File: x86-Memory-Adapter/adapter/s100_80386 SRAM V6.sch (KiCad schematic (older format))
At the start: 71 parts, among them P1 CONN_1, P10 CPLD SPARE, P2 CONN_1, P20 S100_MALE, P3 CONN_1, P34 CONN_1, P35 CONN_1, P4 CONN_1, P5 CONN_20X2, P6 CONN_25X2, P7 XILINX CABLE2, P8 CONN_20X2, P9 CONN_20X2, U1 LDO_REG_7805, U10 74LVX3245, U11 74LVX3245, U12 74LVX3245, U13 74LVX3245, U14 XC9572XL-VQ44, U17 74F04, U2 74LVC573, U3 74LVC573, U4 74LVC573, U5 74LVC573, U6 74LVC573, U7 LM1086CS_TO252_DPAK, U8 74F14, U9 74LVX3245

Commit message: x86-Memory-Adapter: adapter JTAG chain jumper, mezzanine JTAG, CPLD spare header
Source: S100 4GB DRAM BOARD/S100 80386 SRAM DB Version 1/backups/24-04-2015 1921
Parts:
- removed P10: CPLD SPARE, symbol CONN_4
- added P10: CPLD Spare, ~, symbol CONN_2
- added P11: CONN_2X2, symbol CONN_2X2
- added P12: JTAG CHAIN, symbol CONN_2X2
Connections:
- net labels added: FPGA_TDI, FPGA_TDO, TDO_1
- wire segments 713 -> 718
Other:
- note added: "Bridge 2-4 if only CPLD in chain\nBridge 1-2 & 3-4 if FPGA board in chain"
- moved on the sheet: R8, R9
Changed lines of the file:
@@
 Sheet 1 1
 Title "noname.sch"
-Date "23 apr 2015"
+Date "24 apr 2015"
 Rev ""
 Comp ""
@@
 GND
 Text Label 10800 19500 0    60   ~ 0
-CPLD1_TDO
+TDO_1
 Text Label 10800 19600 0    60   ~ 0
 CPLD1_TDI
@@
 	18000 16600 18350 16600
 Wire Wire Line
-	21800 17200 22350 17200
-Wire Wire Line
 	9750 19600 9000 19600
 Wire Wire Line
@@
 Wire Wire Line
 	13250 4450 13100 4450
-Text Label 23050 17200 0    60   ~ 0
+Text Label 22750 18400 0    60   ~ 0
 V3.3
 Text Label 21950 15150 0    60   ~ 0
@@
 V3.3
 Wire Wire Line
-	19800 18150 19800 19350
-Wire Wire Line
 	19500 18150 19500 18450
 Wire Wire Line
@@
 Text Label 17750 14550 2    60   ~ 0
 CPLD_P34
-Text Label 15950 9550 2    60   ~ 0
+Text Label 16650 9550 2    60   ~ 0
 CPLD_P44
 Text Label 14250 13350 0    60   ~ 0
@@
 Text Label 17750 17200 2    60   ~ 0
 CPLD_P8
-Text Label 15950 9250 2    60   ~ 0
-CPLD_P7
 Text Label 11700 5150 2    60   ~ 0
-CPLD_P6
+CPLD_P7
 Text Label 11700 5050 2    60   ~ 0
-CPLD_P5
+CPLD_P6
 Text Label 11700 4950 2    60   ~ 0
-CPLD_P3
+CPLD_P5
 Text Label 11700 4850 2    60   ~ 0
+CPLD_P3
+Text Label 11700 4750 2    60   ~ 0
 CPLD_P2
 Text Label 14250 11050 0    60   ~ 0
 CPLD_P1
-Text Label 15950 9350 2    60   ~ 0
+Text Label 13800 5150 0    60   ~ 0
 CPLD_P8
 Text Label 17750 19150 2    60   ~ 0
@@
 Text Label 22750 16150 0    60   ~ 0
 CPLD_P33
-Text Label 15950 9450 2    60   ~ 0
+Text Label 16650 9350 2    60   ~ 0
 CPLD_P23
 Text Label 20650 12050 2    60   ~ 0
@@
 	13850 13350 14250 13350
 Wire Wire Line
-	11700 4850 12300 4850
+	11700 4750 12300 4750
 Wire Wire Line
-	12300 4950 11700 4950
+	12300 4850 11700 4850
 Wire Wire Line
-	11700 5050 12300 5050
+	11700 4950 12300 4950
 Wire Wire Line
-	12300 5150 11700 5150
-$Comp
-L CONN_4 P10
-U 1 1 5539C2C9
-P 16550 9400
-F 0 "P10" V 16500 9400 50  0000 C CNN
-F 1 "CPLD SPARE" V 16600 9400 50  0000 C CNN
-F 2 "" H 16550 9400 60  0000 C CNN
-F 3 "" H 16550 9400 60  0000 C CNN
-	1    16550 9400
-	1    0    0    -1
-$EndComp
+	12300 5050 11700 5050
 Wire Wire Line
-	16200 9250 15950 9250
+	11700 5150 12300 5150
 Wire Wire Line
-	15950 9350 16200 9350
+	13100 5150 13800 5150
 Wire Wire Line
-	16200 9450 15950 9450
+	16900 9350 16650 9350
 Wire Wire Line
-	15950 9550 16200 9550
+	16650 9550 16900 9550
 $Comp
 L CP C33
@@
 L R R8
 U 1 1 553A0DDD
-P 21550 15150
-F 0 "R8" V 21630 15150 50  0000 C CNN
-F 1 "3v" V 21550 15150 50  0000 C CNN
-F 2 "" H 21550 15150 60  0001 C CNN
-F 3 "" H 21550 15150 60  0001 C CNN
-	1    21550 15150
+P 21500 14950
+F 0 "R8" V 21580 14950 50  0000 C CNN
+F 1 "3v" V 21500 14950 50  0000 C CNN
+F 2 "" H 21500 14950 60  0001 C CNN
+F 3 "" H 21500 14950 60  0001 C CNN
+	1    21500 14950
 	0    1    1    0
 $EndComp
-Wire Wire Line
-	21300 15150 20700 15150
-Wire Wire Line
-	21950 15150 21800 15150
 $Comp
 L R R9
 U 1 1 553A1441
-P 22600 17200
-F 0 "R9" V 22680 17200 50  0000 C CNN
-F 1 "3v" V 22600 17200 50  0000 C CNN
-F 2 "" H 22600 17200 60  0001 C CNN
-F 3 "" H 22600 17200 60  0001 C CNN
-	1    22600 17200
+P 22250 18750
+F 0 "R9" V 22330 18750 50  0000 C CNN
+F 1 "3v" V 22250 18750 50  0000 C CNN
+F 2 "" H 22250 18750 60  0001 C CNN
+F 3 "" H 22250 18750 60  0001 C CNN
+	1    22250 18750
 	0    1    1    0
 $EndComp
 Wire Wire Line
-	23050 17200 22850 17200
-Wire Wire Line
-	19800 19850 19800 20000
-Wire Wire Line
 	9500 20550 9500 20500
 Connection ~ 9500 20500
@@
 Text Label 11850 21000 0    60   ~ 0
 GND
+Text Label 21750 21050 2    60   ~ 0
+CPLD1_TCK
+Text Label 21750 20900 2    60   ~ 0
+CPLD1_TMS
+Text Label 21550 20500 2    60   ~ 0
+FPGA_TDI
+Text Label 22700 20500 0    60   ~ 0
+CPLD1_TDO
+Text Label 22700 20400 0    60   ~ 0
+TDO_1
+$Comp
+L CONN_2X2 P12
+U 1 1 553A766D
+P 22100 20450
+F 0 "P12" H 22100 20600 50  0000 C CNN
+F 1 "JTAG CHAIN" H 22110 20320 40  0000 C CNN
+F 2 "" H 22100 20450 60  0000 C CNN
+F 3 "" H 22100 20450 60  0000 C CNN
+	1    22100 20450
+	1    0    0    -1
+$EndComp
+Text Label 21550 20400 2    60   ~ 0
+FPGA_TDO
+Wire Wire Line
+	22700 20400 22500 20400
+Wire Wire Line
+	22700 20500 22500 20500
+Wire Wire Line
+	21700 20400 21550 20400
+Wire Wire Line
+	21550 20500 21700 20500
+Text Notes 21500 20050 0    60   ~ 0
+Bridge 2-4 if only CPLD in chain\nBridge  1-2 & 3-4 if FPGA board in chain
+Text Label 13100 5700 0    60   ~ 0
+CPLD1_TCK
+Text Label 13100 5600 0    60   ~ 0
+CPLD1_TMS
+Text Label 12150 5700 2    60   ~ 0
+FPGA_TDI
+Text Label 12150 5600 2    60   ~ 0
+FPGA_TDO
+Wire Wire Line
+	12300 5600 12150 5600
+Wire Wire Line
+	12150 5700 12300 5700
+$Comp
+L CONN_2X2 P11
+U 1 1 553A8739
+P 12700 5650
+F 0 "P11" H 12700 5800 50  0000 C CNN
+F 1 "CONN_2X2" H 12710 5520 40  0000 C CNN
+F 2 "" H 12700 5650 60  0000 C CNN
+F 3 "" H 12700 5650 60  0000 C CNN
+	1    12700 5650
+	1    0    0    -1
+$EndComp
+Wire Wire Line
+	21800 17200 21900 17200
+Wire Wire Line
+	21900 17200 21900 18400
+Wire Wire Line
+	19800 18400 22750 18400
+Wire Wire Line
+	19800 18400 19800 18150
+Connection ~ 21900 18400
+Wire Wire Line
+	20700 15150 21950 15150
+$Comp
+L CONN_2 P10
+U 1 1 553AB388
+P 17250 9450
+F 0 "P10" V 17200 9450 40  0000 C CNN
+F 1 "CPLD Spare" V 17300 9450 40  0000 C CNN
+F 2 "~" H 17250 9450 60  0000 C CNN
+F 3 "~" H 17250 9450 60  0000 C CNN
+	1    17250 9450
+	1    0    0    -1
+$EndComp
 $EndSCHEMATC

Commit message: x86-Memory-Adapter: adapter LT3081 adjustable rail and 3.3V/5V source jumpers; first routing
Source: S100 4GB DRAM BOARD/S100 80386 SRAM DB Version 1/backups/25-04-2015 1211
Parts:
- added C12, C16, C2, C20, C23, C25, C5: 10 uF, symbol CP
- added K1: 3.3V, ~, symbol CONN_3
- added K2: 5V, ~, symbol CONN_3
- added P13: LT Output select, symbol CONN_6X2
- added R10: 500, symbol R
- added R11: 24.3K, symbol R
- added R12: 36.5K, symbol R
- added R13: 66.5K, symbol R
- added R14: 100, symbol R
- added R15: 30.1K, symbol R
- added R16: 49.9K, symbol R
- added R17: 100K, symbol R
- added R7: 4.53k, symbol R
- added U15: LDO_REG_7805, ~, symbol LDO_REG_7805
- added U16: LM1086CS, symbol LM1086CS
- added U18, U19: POWER_SELECT, symbol POWER_SELECT
- added U20: LT3081-TSSOP16, symbol LT3081-TSSOP16
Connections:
- net labels added: LM1086 out, LM7805 out, LTout
- wire segments 718 -> 825
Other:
- note added: "+3.3V from Power supply on Rail"
- note added: "+5V from Power supply on Rail"
- note added: "Optional"

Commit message: x86-Memory-Adapter: adapter power section simplified; routed board and gerbers
Source: S100 4GB DRAM BOARD/S100 80386 SRAM DB Version 1/backups/20-06-2015 1159 - need to move CPLD
The folder was made on 20-06-2015 but its files were last saved on 25-04-2015 (gerbers 14:47), so the commit carries the April date.
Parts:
- removed C2, C5: 10 uF, symbol CP
- removed R8, R9: 3v, symbol R
- removed U15: LDO_REG_7805, ~, symbol LDO_REG_7805
- removed U16: LM1086CS, symbol LM1086CS
- removed U18, U19: POWER_SELECT, symbol POWER_SELECT
- added R18: 300, symbol R
- R14: value 100 -> 1K
- U20: value LT3081-TSSOP16 -> LT3081
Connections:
- wire segments 825 -> 802
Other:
- note added: "TSSOP16"
- note removed: "+3.3V from Power supply on Rail"
- note removed: "+5V from Power supply on Rail"

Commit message: x86-Memory-Adapter: adapter CPLD moved to bottom; add general I/O, 23LC1024, select LED
Source: S100 4GB DRAM BOARD/S100 80386 SRAM DB Version 1/backups/21-06-2015 1724
Board partly re-routed after the move. The April gerbers are kept.
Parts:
- added C2: 0.1 uF, symbol C
- added D2: LED, LEDV, symbol LED
- added P14: GenIO_1, symbol CONN_6X2
- added P15: GenIO_2, symbol CONN_6X2
- added R19: 10k, symbol R
- added R20: 1K, symbol R
- added R21, R22, R23, R9: 10K, symbol R
- added R8: 330, symbol R
- added U15: ZZZZ1, symbol ZZZZ1
- added U16: ^^74LV244, ~, symbol ^^74LV244
- added U18: 23LC1024, symbol 23LC1024
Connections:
- net labels added: 23LC_CLKa, 23LC_CLKb, 23LC_CS, 23LC_CSa, 23LC_CSb, 23LC_Dina, 23LC_Dinb, 23LC_Douta, 23LC_Doutb, 23LC_OEa, 23LC_OEb, GenIO_1, GenIO_10, GenIO_11, GenIO_2, GenIO_3, GenIO_4, GenIO_5, GenIO_6, GenIO_7, GenIO_8, GenIO_9
- wire segments 802 -> 901
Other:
- note added: "FPGA side (OEa)"
- note added: "General I/O on Daughter Board \n to Breakout Cable Connector"
- note added: "SN74LV244ADWR\nRS Stock No.662-8477"
- note added: "off board IO side (OEb)"

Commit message: x86-Memory-Adapter: adapter LM2596 buck pre-regulator for the LT3081
Source: S100 4GB DRAM BOARD/S100 80386 SRAM DB Version 1/backups/17-07-2015 2113
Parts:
- added D3: SMALL_DIODE_SCHOTTKY, symbol SMALL_DIODE_SCHOTTKY
- added L1: SMALL_INDUCTANCE, symbol SMALL_INDUCTANCE
- added R24: 470, symbol R
- added U19: LM2596, symbol LM2596
- added VR1: VR1, ~, symbol VR1
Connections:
- net labels added: LM2596output
- wire segments 901 -> 922
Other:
- note added: "10K Trimmer"
- note added: "LT3081 Buck"
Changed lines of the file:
@@
 	25650 7650 25500 7650
 Wire Notes Line
-	-16550 -1100 -10850 -1100
-Wire Notes Line
-	-16550 1450 -16550 -1100
+	-16550 -1100 -7050 -1100
+Wire Notes Line
+	-16550 -1100 -16550 7400
 Text Notes -15100 -800 0    99   ~ 0
 General I/O on Daughter Board \n   to Breakout Cable Connector
@@
 Text Notes -13850 6700 0    60   ~ 0
 SN74LV244ADWR\nRS Stock No.662-8477
+Wire Notes Line
+	6950 17000 11450 17000
+Wire Notes Line
+	11450 17000 11450 12000
+Wire Notes Line
+	11450 12000 6950 12000
+Wire Notes Line
+	6950 12000 6950 17000
+Text Notes 10100 12200 0    60   ~ 0
+LT3081 Buck
+Wire Notes Line
+	-7050 -1100 -7050 7400
+Wire Notes Line
+	-7050 7400 -16550 7400
+$Comp
+L LM2596 U19
+U 1 1 5587703D
+P -7650 13500
+F 0 "U19" H -7950 14050 60  0000 C CNN
+F 1 "LM2596" H -7650 13950 60  0000 C CNN
+F 2 "" H -7650 13500 60  0000 C CNN
+F 3 "" H -7650 13500 60  0000 C CNN
+	1    -7650 13500
+	1    0    0    -1
+$EndComp
+$Comp
+L SMALL_INDUCTANCE L1
+U 1 1 55877336
+P -6300 13300
+F 0 "L1" H -6000 13500 30  0000 C CNN
+F 1 "SMALL_INDUCTANCE" H -6000 13350 30  0000 C CNN
+F 2 "" H -6300 13300 60  0000 C CNN
+F 3 "" H -6300 13300 60  0000 C CNN
+	1    -6300 13300
+	1    0    0    -1
+$EndComp
+Wire Wire Line
+	-6850 13200 -6250 13200
+$Comp
+L SMALL_DIODE_SCHOTTKY D3
+U 1 1 55877BDC
+P -6250 13900
+F 0 "D3" H -5750 14150 30  0000 C CNN
+F 1 "SMALL_DIODE_SCHOTTKY" H -5900 13950 30  0000 C CNN
+F 2 "" H -6250 13900 60  0000 C CNN
+F 3 "" H -6250 13900 60  0000 C CNN
+	1    -6250 13900
+	0    -1   -1   0
+$EndComp
+Wire Wire Line
+	-5750 13200 -5400 13200
+Wire Wire Line
+	-6850 13650 -6700 13650
+Connection ~ -5550 13200
+Wire Wire Line
+	-6450 13200 -6450 13350
+Connection ~ -6450 13200
+Wire Wire Line
+	-6450 14300 -6450 13750
+Wire Wire Line
+	-8600 14300 -6450 14300
+Wire Wire Line
+	-7650 14300 -7650 14200
+Wire Wire Line
+	-8450 13400 -8600 13400
+Wire Wire Line
+	-8600 13400 -8600 14300
+Connection ~ -7650 14300
+Text Label -7450 14500 0    60   ~ 0
+GND
+Wire Wire Line
+	-7500 14300 -7500 14500
+Wire Wire Line
+	-7500 14500 -7450 14500
+Connection ~ -7500 14300
+Text Label -8750 13200 2    60   ~ 0
++8Vi
+Wire Wire Line
+	-8750 13200 -8450 13200
+$Comp
+L VR1 VR1
+U 1 1 55865F71
+P -5550 13700
+F 0 "VR1" H -5720 13800 50  0000 C CNN
+F 1 "VR1" V -5550 13700 50  0000 C CNN
+F 2 "~" H -5550 13700 60  0000 C CNN
+F 3 "~" H -5550 13700 60  0000 C CNN
+	1    -5550 13700
+	1    0    0    -1
+$EndComp
+Wire Wire Line
+	-5550 13200 -5550 13450
+$Comp
+L R R24
+U 1 1 558663D9
+P -5550 14350
+F 0 "R24" V -5470 14350 50  0000 C CNN
+F 1 "470" V -5550 14350 50  0000 C CNN
+F 2 "" H -5550 14350 60  0001 C CNN
+F 3 "" H -5550 14350 60  0001 C CNN
+	1    -5550 14350
+	1    0    0    -1
+$EndComp
+Text Label -5450 14700 0    60   ~ 0
+GND
+Wire Wire Line
+	-5550 14600 -5550 14700
+Wire Wire Line
+	-5550 14700 -5450 14700
+Wire Wire Line
+	-6700 13650 -6700 14000
+Wire Wire Line
+	-6700 14000 -5150 14000
+Wire Wire Line
+	-5550 13950 -5550 14100
+Connection ~ -5550 14000
+Text Label -5400 13200 0    60   ~ 0
+LM2596output
+Wire Wire Line
+	-5400 13700 -5150 13700
+Wire Wire Line
+	-5150 13700 -5150 14000
+Text Notes -5350 13650 0    60   ~ 0
+10K Trimmer
+Wire Wire Line
+	-7850 14200 -7850 14300
+Connection ~ -7850 14300
 $EndSCHEMATC

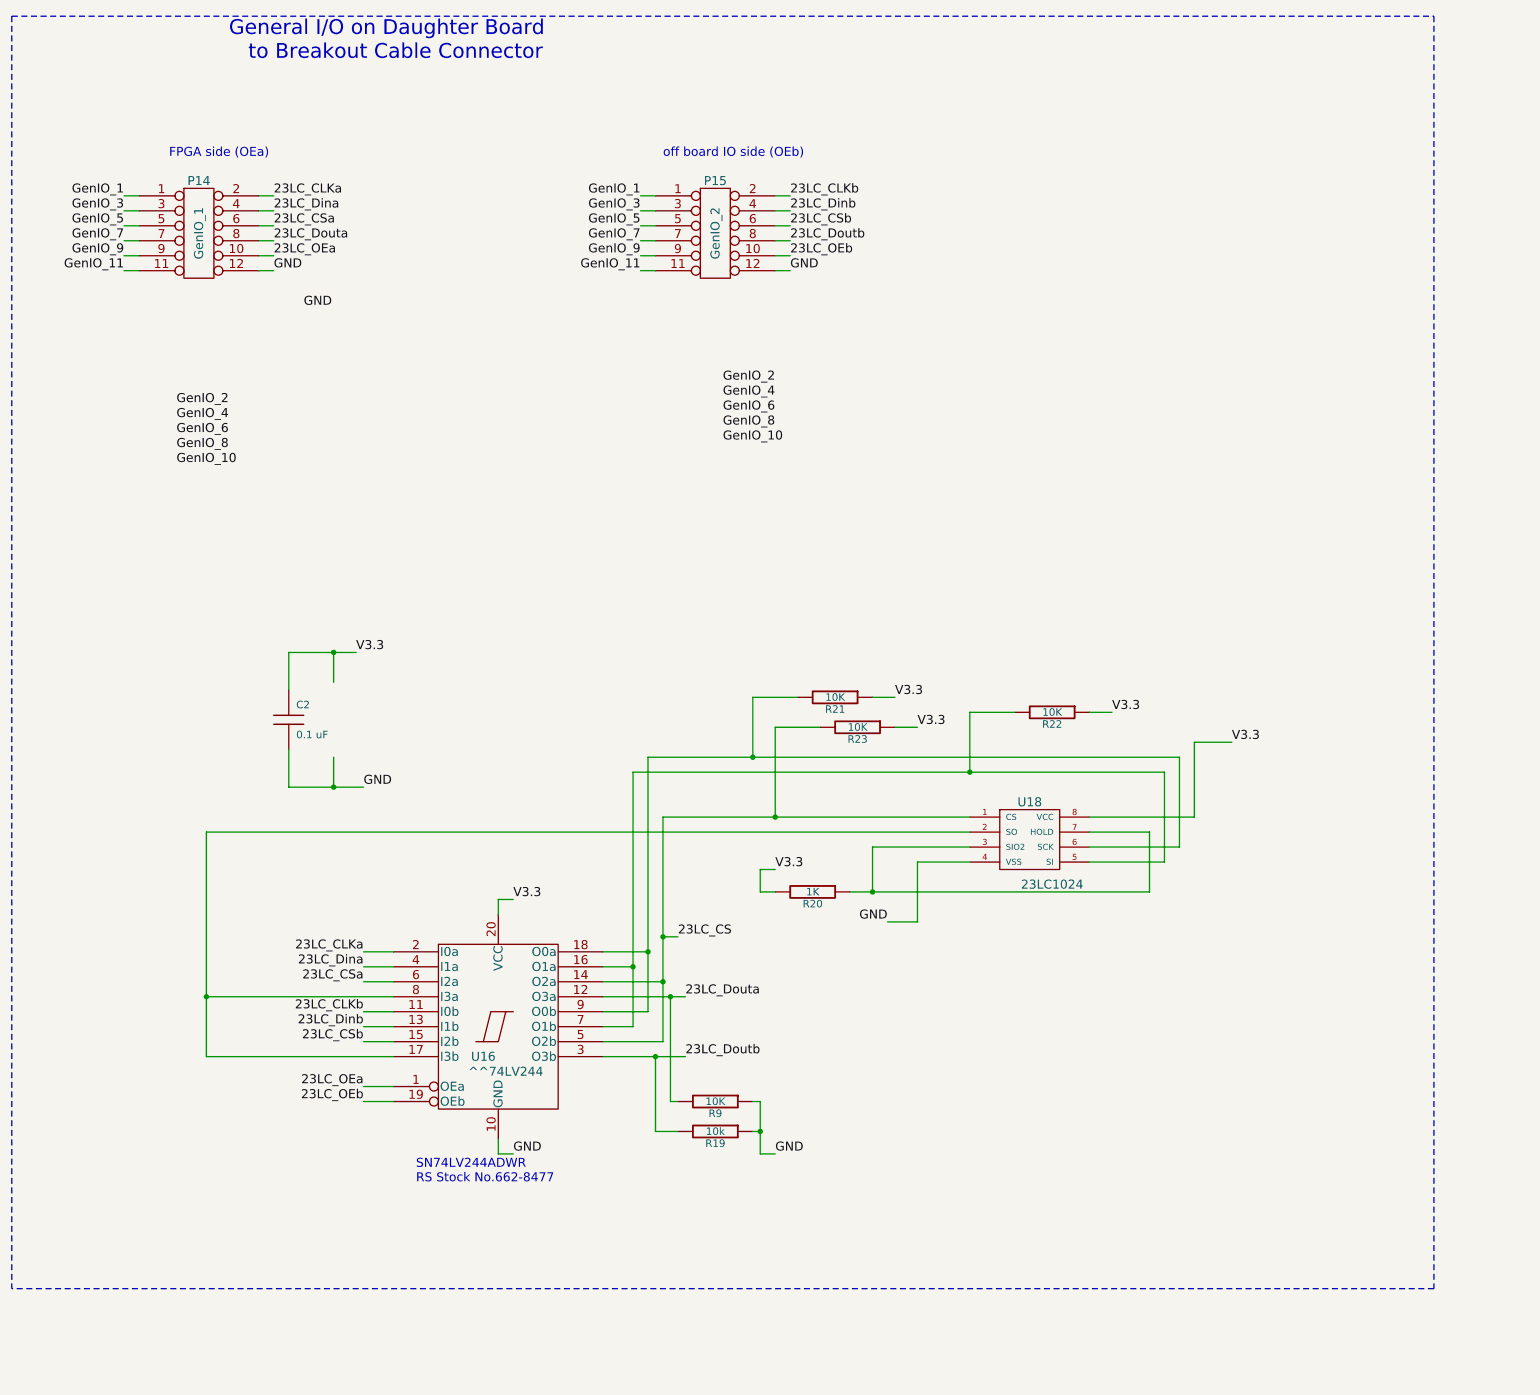
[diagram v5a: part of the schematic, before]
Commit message: x86-Memory-Adapter: adapter general I/O and SPI SRAM removed; board re-routed
Source: S100 4GB DRAM BOARD/S100 80386 SRAM DB Version 1 (working folder)
No gerbers were made from this final layout; GERBERS/ is the April 2015 plot.
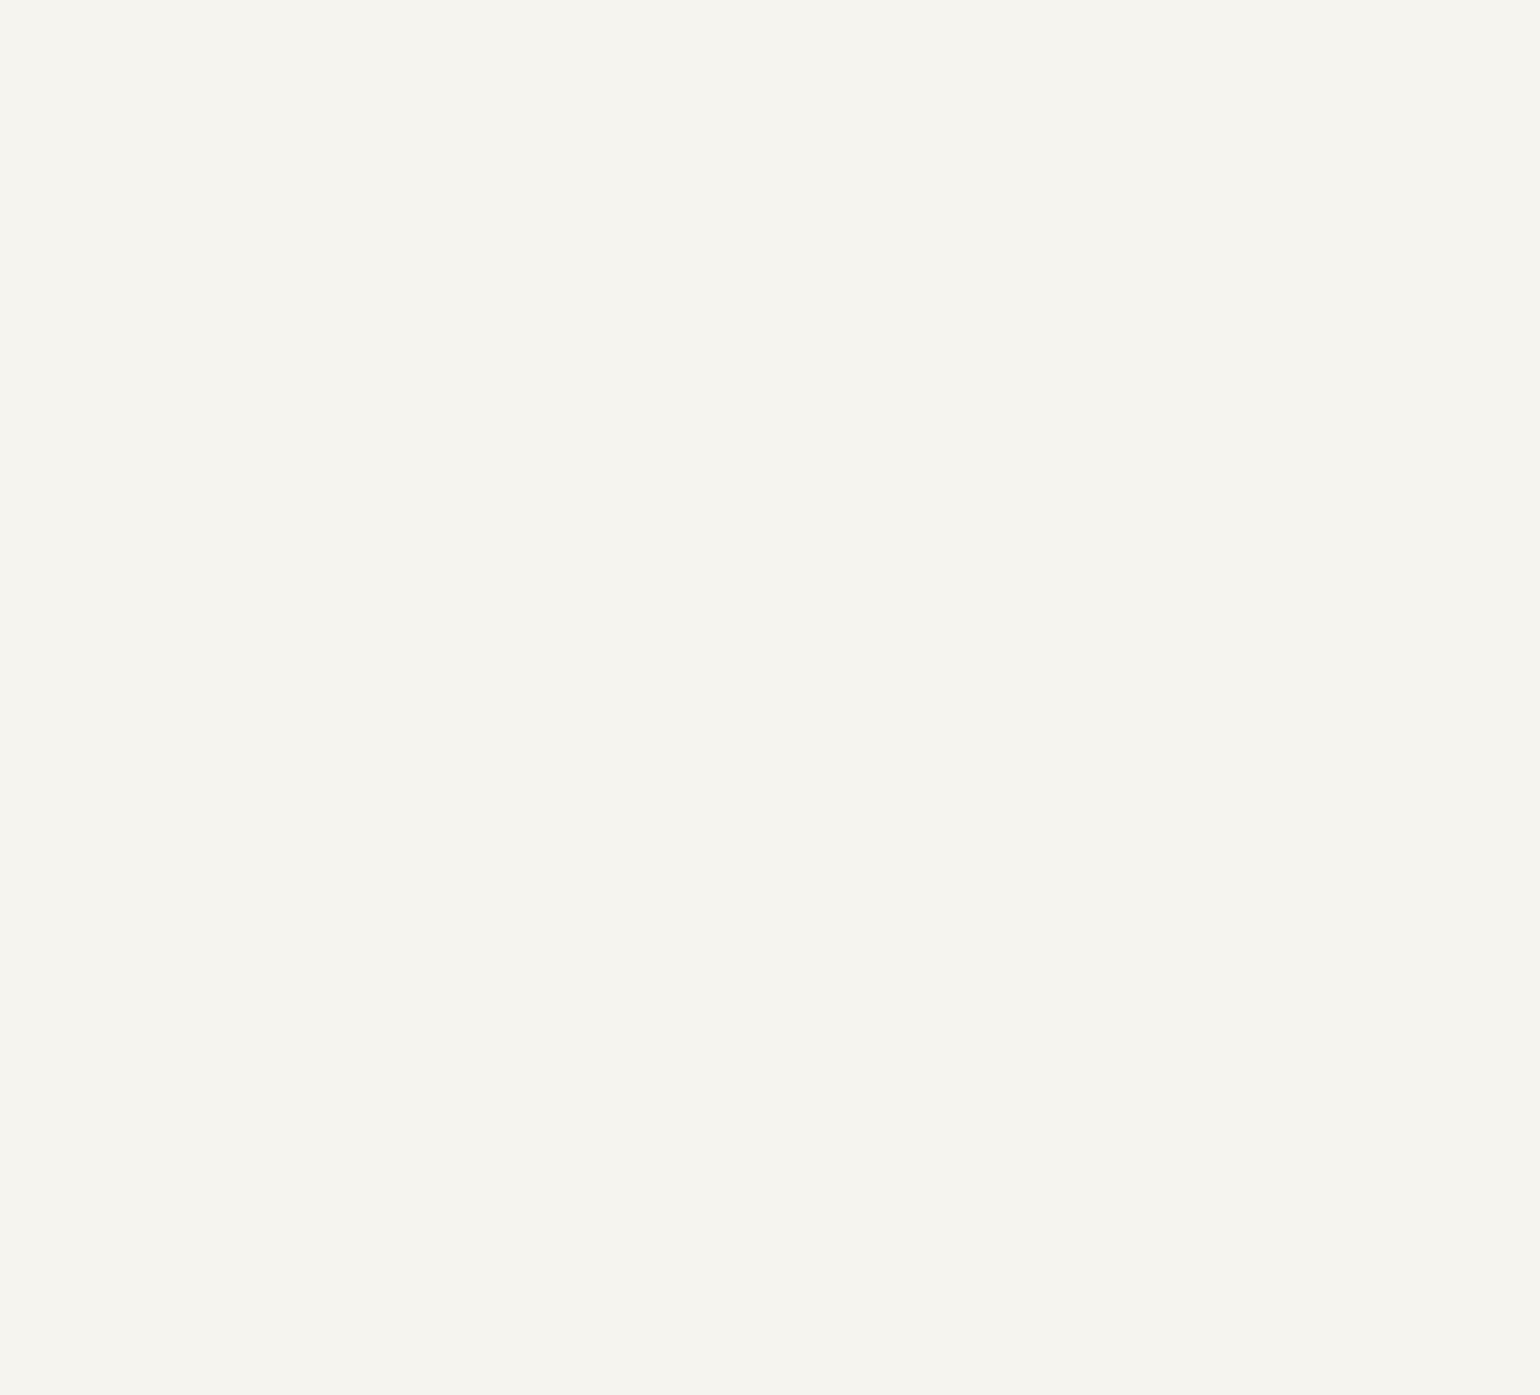
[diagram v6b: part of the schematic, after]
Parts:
- removed C2: 0.1 uF, symbol C
- removed P14: GenIO_1, symbol CONN_6X2
- removed P15: GenIO_2, symbol CONN_6X2
- removed R19: 10k, symbol R
- removed R20: 1K, symbol R
- removed R21, R22, R23, R9: 10K, symbol R
- removed U16: ^^74LV244, ~, symbol ^^74LV244
- removed U18: 23LC1024, symbol 23LC1024
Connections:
- net labels removed: 23LC_CLKa, 23LC_CLKb, 23LC_CS, 23LC_CSa, 23LC_CSb, 23LC_Dina, 23LC_Dinb, 23LC_Douta, 23LC_Doutb, 23LC_OEa, 23LC_OEb, GenIO_1, GenIO_10, GenIO_11, GenIO_2, GenIO_3, GenIO_4, GenIO_5, GenIO_6, GenIO_7, GenIO_8, GenIO_9
- wire segments 922 -> 826
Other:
- note removed: "FPGA side (OEa)"
- note removed: "General I/O on Daughter Board \n to Breakout Cable Connector"
- note removed: "SN74LV244ADWR\nRS Stock No.662-8477"
- note removed: "off board IO side (OEb)"
